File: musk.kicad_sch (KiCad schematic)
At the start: 56 parts, among them J1 debug-port, J10 Conn_01x06_Male, J3 Conn_01x06_Male, J4 Conn_01x06_Male, J5 Conn_01x06_Male, J6 Conn_01x06_Male, J7 Conn_01x06_Male, J8 Conn_01x06_Male, J9 Conn_01x06_Male, K1 diode-choc, K10 diode-choc, K11 diode-choc, K12 diode-choc, K13 diode-choc, K14 diode-choc, K15 diode-choc, K16 diode-choc, K2 diode-choc, K3 diode-choc, K4 diode-choc, K5 diode-choc, K6 diode-choc, K7 diode-choc, K8 diode-choc, K9 diode-choc, SW1 SW_Push, SW2 RotaryEncoder, U1 MT25QL128ABA1ESE, U2 ms88sf3-nrf52840, U3 LSM6DS3, U8 PMW3610, U9 MCP1804x-1802xMB

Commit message: done
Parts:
- removed H1, H2, H3, H4: bumpon, fusion:bumpon-sunk-hole, symbol Mechanical:MountingHole
- removed SC1: solar, misc:KXOB25-05X3F, symbol Device:Solar_Cell
- added JP2: left right or all, Jumper:SolderJumper-3_P1.3mm_Open_RoundedPad1.0x1.5mm, symbol Jumper:SolderJumper_3_Open
- added K17: diode-choc, pg1232:pg1232-DC, symbol switch:diode-choc
- JP1: value All or none -> left right or all
- K13: footprint pg1232:pg1232-DSS -> pg1232:pg1232-DC
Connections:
- net +3V3: now also JP1.2 (C), JP2.3 (B); no longer JP1.1 (A)
- net 3V3_nRF: now also JP1.1 (A)
- net C0: now also K13.2; no longer J5.1 (Pin_1)
- net GND: now also J5.2 (Pin_2); no longer J8.6 (Pin_6), SW1.2
- net R3: now also J8.4 (Pin_4), K13.1, U2.40 (P0.15); no longer J5.2 (Pin_2), J8.3 (Pin_3), U2.41 (P0.17)
- net SOLAR: no longer J8.5 (Pin_5)
- net SOLAR_OUT: now also U9.3 (IN), JP2.1 (A)
- net VDDH: now also JP2.2 (C); no longer JP1.2 (C), U9.3 (IN)
- net ~{BLUE}: now also U2.17 (P0.26); no longer U2.15 (A3_P0.05)
- net ~{RED}: now also U2.15 (A3_P0.05); no longer U2.17 (P0.26)
- net at J9.3 (Pin_3), K16.1: now also K17.1
- net at K16.2: now also J9.5 (Pin_5); no longer J9.2 (Pin_2)
- net at J3.3 (Pin_3): now also J6.4 (Pin_4); no longer J6.3 (Pin_3)
- net at J3.4 (Pin_4): now also J6.3 (Pin_3); no longer J6.4 (Pin_4)
- net at J6.5 (Pin_5): now also J3.2 (Pin_2); no longer J3.5 (Pin_5)
- net at J6.6 (Pin_6): now also J3.1 (Pin_1); no longer J3.6 (Pin_6)
- net at SW1.1: now also J3.6 (Pin_6), J6.1 (Pin_1); no longer U2.28 (P0.18/RST)
- net at J10.3 (Pin_3), K15.1: now also J7.4 (Pin_4); no longer J7.3 (Pin_3)
- net at J7.1 (Pin_1), K15.2: now also J10.6 (Pin_6); no longer J10.1 (Pin_1)
- net at J9.4 (Pin_4): now also K17.2
- net at J10.2 (Pin_2): now also J7.5 (Pin_5); no longer J7.2 (Pin_2)
- net at J10.4 (Pin_4): now also J7.3 (Pin_3)
- net at J10.5 (Pin_5): now also J7.2 (Pin_2); no longer J7.5 (Pin_5)
- net at J7.6 (Pin_6): now also J10.1 (Pin_1); no longer J10.6 (Pin_6)
- new net: J3.5 (Pin_5), J6.2 (Pin_2), SW1.2
- new net C4: J8.3 (Pin_3), U2.41 (P0.17)
- new net RST: J5.1 (Pin_1), U2.28 (P0.18/RST)
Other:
- sheet power ports: added SOLAR; removed VDDH
- note added: "JP1 JP2 12 12 # some DC/DC, some LDO 23 12 # all use builtin DC/DC 123 23 # all using LDO"
- note removed: "- capacitive for hand detection"
- moved on the sheet: C10, C11, C12, C13, C14, C15, J10, JP1, K13, SW1, U8, U9

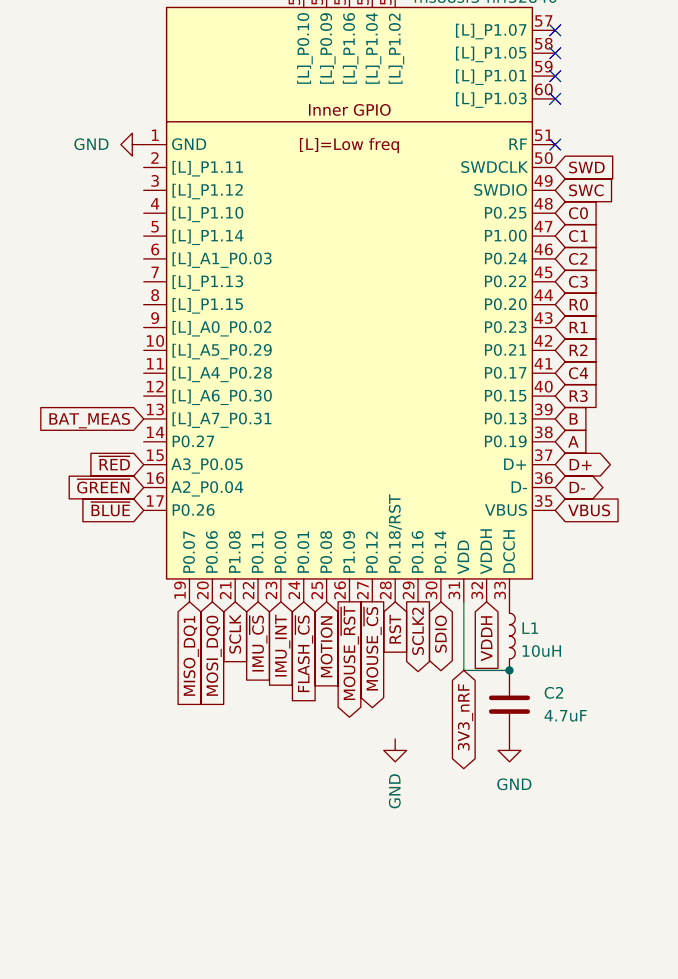
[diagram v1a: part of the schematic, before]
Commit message: 5 thumb cluster
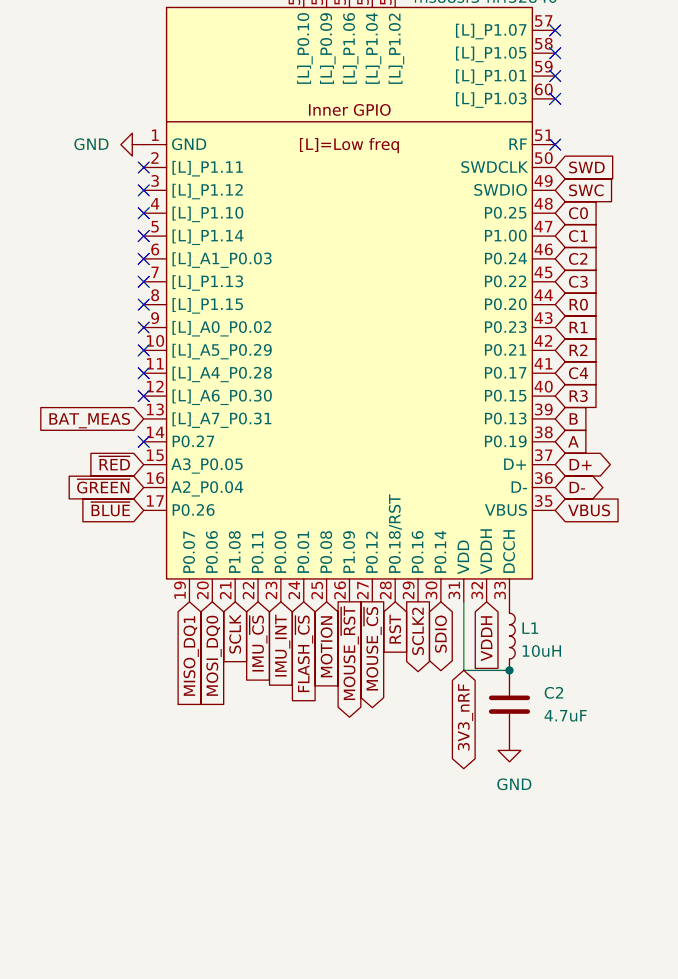
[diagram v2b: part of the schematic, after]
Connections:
- no-connect marks 18 -> 30
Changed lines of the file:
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@@
   (no_connect (at 74.93 29.21))
   (no_connect (at 209.55 110.49))
+  (no_connect (at 29.21 67.31))
+  (no_connect (at 29.21 69.85))
   (no_connect (at 57.15 24.13))
+  (no_connect (at 29.21 52.07))
+  (no_connect (at 29.21 74.93))
+  (no_connect (at 29.21 59.69))
+  (no_connect (at 29.21 44.45))
   (no_connect (at 54.61 24.13))
   (no_connect (at 130.81 124.46))
   (no_connect (at 246.38 120.65))
+  (no_connect (at 29.21 57.15))
   (no_connect (at 269.24 120.65))
   (no_connect (at 52.07 24.13))
+  (no_connect (at 29.21 54.61))
   (no_connect (at 74.93 31.75))
+  (no_connect (at 29.21 62.23))
   (no_connect (at 46.99 24.13))
+  (no_connect (at 29.21 64.77))
   (no_connect (at 74.93 41.91))
   (no_connect (at 74.93 36.83))
@@
   (no_connect (at 269.24 110.49))
   (no_connect (at 209.55 113.03))
+  (no_connect (at 29.21 46.99))
   (no_connect (at 269.24 123.19))
   (no_connect (at 246.38 123.19))
   (no_connect (at 49.53 24.13))
+  (no_connect (at 29.21 49.53))
   (wire (pts (xy 269.24 115.57) (xy 280.67 115.57))
     (stroke (width 0) (type default) (color 0 0 0 0))
@@
     (pin "2")
   )
-  (symbol (lib_id "power:GND") (at 57.15 107.95 0) (unit 1)
-    (in_bom yes) (on_board yes)
-    (property "Reference" "#PWR05" (id 0) (at 57.15 114.3 0)
-      (effects (font (size 1.27 1.27)) hide)
-    )
-    (property "Value" "GND" (id 1) (at 57.15 111.76 90)
-      (effects (font (size 1.27 1.27)) (justify right))
-    )
-    (property "Footprint" "" (id 2) (at 57.15 107.95 0)
-      (effects (font (size 1.27 1.27)) hide)
-    )
-    (property "Datasheet" "" (id 3) (at 57.15 107.95 0)
-      (effects (font (size 1.27 1.27)) hide)
-    )
-    (pin "1")
-  )
   (symbol (lib_id "switch:diode-choc") (at 180.34 132.08 0) (unit 1)
     (in_bom yes) (on_board yes)
@@
       (reference "#PWR04") (unit 1) (value "GND") (footprint "")
     )
-    (path "/9c3a6b82-7222-44b1-a8fb-55963f13e302"
-      (reference "#PWR05") (unit 1) (value "GND") (footprint "")
-    )
     (path "/ee3392d2-a129-45fe-8b02-43c63760b23d"

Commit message: hotswap choc mini
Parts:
- K1, K5, K9: footprint pg1232:pg1232-DCR -> pg1232:pg1232-DHCR
- K10, K13, K14, K15, K16, K17, K2, K6: footprint pg1232:pg1232-DC -> pg1232:pg1232-DHC
- K11, K3, K7: footprint pg1232:pg1232-DCL -> pg1232:pg1232-DHCL
- K12, K4, K8: footprint pg1232:pg1232-DCN -> pg1232:pg1232-DHCN
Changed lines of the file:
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@@
       (effects (font (size 1.27 1.27)) (justify left) hide)
     )
-    (property "Footprint" "pg1232:pg1232-DC" (id 2) (at 278.13 105.41 0)
+    (property "Footprint" "pg1232:pg1232-DHC" (id 2) (at 278.13 105.41 0)
       (effects (font (size 1.27 1.27)) hide)
     )
@@
       (effects (font (size 1.27 1.27)) (justify left) hide)
     )
-    (property "Footprint" "pg1232:pg1232-DC" (id 2) (at 284.48 114.3 0)
+    (property "Footprint" "pg1232:pg1232-DHC" (id 2) (at 284.48 114.3 0)
       (effects (font (size 1.27 1.27)) hide)
     )
@@
       (effects (font (size 1.27 1.27)) (justify left) hide)
     )
-    (property "Footprint" "pg1232:pg1232-DC" (id 2) (at 153.67 137.16 0)
+    (property "Footprint" "pg1232:pg1232-DHC" (id 2) (at 153.67 137.16 0)
       (effects (font (size 1.27 1.27)) hide)
     )
@@
       (effects (font (size 1.27 1.27)) (justify left) hide)
     )
-    (property "Footprint" "pg1232:pg1232-DCR" (id 2) (at 153.67 128.27 0)
+    (property "Footprint" "pg1232:pg1232-DHCR" (id 2) (at 153.67 128.27 0)
       (effects (font (size 1.27 1.27)) hide)
     )
@@
       (effects (font (size 1.27 1.27)) (justify left) hide)
     )
-    (property "Footprint" "pg1232:pg1232-DC" (id 2) (at 261.62 100.33 0)
+    (property "Footprint" "pg1232:pg1232-DHC" (id 2) (at 261.62 100.33 0)
       (effects (font (size 1.27 1.27)) hide)
     )
@@
       (effects (font (size 1.27 1.27)) (justify left) hide)
     )
-    (property "Footprint" "pg1232:pg1232-DCN" (id 2) (at 180.34 119.38 0)
+    (property "Footprint" "pg1232:pg1232-DHCN" (id 2) (at 180.34 119.38 0)
       (effects (font (size 1.27 1.27)) hide)
     )
@@
       (effects (font (size 1.27 1.27)) (justify left) hide)
     )
-    (property "Footprint" "pg1232:pg1232-DCR" (id 2) (at 153.67 110.49 0)
+    (property "Footprint" "pg1232:pg1232-DHCR" (id 2) (at 153.67 110.49 0)
       (effects (font (size 1.27 1.27)) hide)
     )
@@
       (effects (font (size 1.27 1.27)) (justify left) hide)
     )
-    (property "Footprint" "pg1232:pg1232-DCN" (id 2) (at 180.34 128.27 0)
+    (property "Footprint" "pg1232:pg1232-DHCN" (id 2) (at 180.34 128.27 0)
       (effects (font (size 1.27 1.27)) hide)
     )
@@
       (effects (font (size 1.27 1.27)) (justify left) hide)
     )
-    (property "Footprint" "pg1232:pg1232-DCR" (id 2) (at 153.67 119.38 0)
+    (property "Footprint" "pg1232:pg1232-DHCR" (id 2) (at 153.67 119.38 0)
       (effects (font (size 1.27 1.27)) hide)
     )
@@
       (effects (font (size 1.27 1.27)) (justify left) hide)
     )
-    (property "Footprint" "pg1232:pg1232-DC" (id 2) (at 162.56 137.16 0)
+    (property "Footprint" "pg1232:pg1232-DHC" (id 2) (at 162.56 137.16 0)
       (effects (font (size 1.27 1.27)) hide)
     )
@@
       (effects (font (size 1.27 1.27)) (justify left) hide)
     )
-    (property "Footprint" "pg1232:pg1232-DCL" (id 2) (at 171.45 119.38 0)
+    (property "Footprint" "pg1232:pg1232-DHCL" (id 2) (at 171.45 119.38 0)
       (effects (font (size 1.27 1.27)) hide)
     )
@@
       (effects (font (size 1.27 1.27)) (justify left) hide)
     )
-    (property "Footprint" "pg1232:pg1232-DCL" (id 2) (at 171.45 128.27 0)
+    (property "Footprint" "pg1232:pg1232-DHCL" (id 2) (at 171.45 128.27 0)
       (effects (font (size 1.27 1.27)) hide)
     )
@@
       (effects (font (size 1.27 1.27)) (justify left) hide)
     )
-    (property "Footprint" "pg1232:pg1232-DCL" (id 2) (at 171.45 110.49 0)
+    (property "Footprint" "pg1232:pg1232-DHCL" (id 2) (at 171.45 110.49 0)
       (effects (font (size 1.27 1.27)) hide)
     )
@@
       (effects (font (size 1.27 1.27)) (justify left) hide)
     )
-    (property "Footprint" "pg1232:pg1232-DC" (id 2) (at 162.56 110.49 0)
+    (property "Footprint" "pg1232:pg1232-DHC" (id 2) (at 162.56 110.49 0)
       (effects (font (size 1.27 1.27)) hide)
     )
@@
       (effects (font (size 1.27 1.27)) (justify left) hide)
     )
-    (property "Footprint" "pg1232:pg1232-DCN" (id 2) (at 180.34 110.49 0)
+    (property "Footprint" "pg1232:pg1232-DHCN" (id 2) (at 180.34 110.49 0)
       (effects (font (size 1.27 1.27)) hide)
     )
@@
       (effects (font (size 1.27 1.27)) (justify left) hide)
     )
-    (property "Footprint" "pg1232:pg1232-DC" (id 2) (at 162.56 128.27 0)
+    (property "Footprint" "pg1232:pg1232-DHC" (id 2) (at 162.56 128.27 0)
       (effects (font (size 1.27 1.27)) hide)
     )
@@
       (effects (font (size 1.27 1.27)) (justify left) hide)
     )
-    (property "Footprint" "pg1232:pg1232-DC" (id 2) (at 162.56 119.38 0)
+    (property "Footprint" "pg1232:pg1232-DHC" (id 2) (at 162.56 119.38 0)
       (effects (font (size 1.27 1.27)) hide)
     )
@@
     )
     (path "/87bdc01e-a055-4d4c-8488-cd7ca475e086"
-      (reference "K1") (unit 1) (value "diode-choc") (footprint "pg1232:pg1232-DCR")
+      (reference "K1") (unit 1) (value "diode-choc") (footprint "pg1232:pg1232-DHCR")
     )
     (path "/da248da7-bb82-42ca-90ae-06208c9de7f0"
-      (reference "K2") (unit 1) (value "diode-choc") (footprint "pg1232:pg1232-DC")
+      (reference "K2") (unit 1) (value "diode-choc") (footprint "pg1232:pg1232-DHC")
     )
     (path "/d9459f95-47ce-4f40-805c-323d6f49037e"
-      (reference "K3") (unit 1) (value "diode-choc") (footprint "pg1232:pg1232-DCL")
+      (reference "K3") (unit 1) (value "diode-choc") (footprint "pg1232:pg1232-DHCL")
     )
     (path "/ec136a70-3607-4003-a7a6-cdc612bb426c"
-      (reference "K4") (unit 1) (value "diode-choc") (footprint "pg1232:pg1232-DCN")
+      (reference "K4") (unit 1) (value "diode-choc") (footprint "pg1232:pg1232-DHCN")
     )
     (path "/a188b754-8ecd-4d74-8170-d4a8926c87ae"
-      (reference "K5") (unit 1) (value "diode-choc") (footprint "pg1232:pg1232-DCR")
+      (reference "K5") (unit 1) (value "diode-choc") (footprint "pg1232:pg1232-DHCR")
     )
     (path "/f92feeaa-c2da-458b-82e9-a07def69cb43"
-      (reference "K6") (unit 1) (value "diode-choc") (footprint "pg1232:pg1232-DC")
+      (reference "K6") (unit 1) (value "diode-choc") (footprint "pg1232:pg1232-DHC")
     )
     (path "/ae452cd4-a096-4b05-9662-460b8817444e"
-      (reference "K7") (unit 1) (value "diode-choc") (footprint "pg1232:pg1232-DCL")
+      (reference "K7") (unit 1) (value "diode-choc") (footprint "pg1232:pg1232-DHCL")
     )
     (path "/7963e912-fe67-47e1-8f51-4cb8ba56eb8c"
-      (reference "K8") (unit 1) (value "diode-choc") (footprint "pg1232:pg1232-DCN")
+      (reference "K8") (unit 1) (value "diode-choc") (footprint "pg1232:pg1232-DHCN")
     )
     (path "/45b4d680-79c6-462d-8620-4846ae703fd9"
-      (reference "K9") (unit 1) (value "diode-choc") (footprint "pg1232:pg1232-DCR")
+      (reference "K9") (unit 1) (value "diode-choc") (footprint "pg1232:pg1232-DHCR")
     )
     (path "/f3d11e68-ea73-47b6-a5c5-7f172924a5ac"
-      (reference "K10") (unit 1) (value "diode-choc") (footprint "pg1232:pg1232-DC")
+      (reference "K10") (unit 1) (value "diode-choc") (footprint "pg1232:pg1232-DHC")
     )
     (path "/cb60c373-da5a-49e5-a01f-0bb47bd19c8a"
-      (reference "K11") (unit 1) (value "diode-choc") (footprint "pg1232:pg1232-DCL")
+      (reference "K11") (unit 1) (value "diode-choc") (footprint "pg1232:pg1232-DHCL")
     )
     (path "/9c60c31c-8d19-4129-96ae-58b8c24f361a"
-      (reference "K12") (unit 1) (value "diode-choc") (footprint "pg1232:pg1232-DCN")
+      (reference "K12") (unit 1) (value "diode-choc") (footprint "pg1232:pg1232-DHCN")
     )
     (path "/360112f0-6f4f-4683-9f67-c30cff64c0d6"
-      (reference "K13") (unit 1) (value "diode-choc") (footprint "pg1232:pg1232-DC")
+      (reference "K13") (unit 1) (value "diode-choc") (footprint "pg1232:pg1232-DHC")
     )
     (path "/abfa173d-9db1-45b6-ad22-b6c38a35afa9"
-      (reference "K14") (unit 1) (value "diode-choc") (footprint "pg1232:pg1232-DC")
+      (reference "K14") (unit 1) (value "diode-choc") (footprint "pg1232:pg1232-DHC")
     )
     (path "/700f52c5-679c-497f-8976-e17d015dbeaa"
-      (reference "K15") (unit 1) (value "diode-choc") (footprint "pg1232:pg1232-DC")
+      (reference "K15") (unit 1) (value "diode-choc") (footprint "pg1232:pg1232-DHC")
     )
     (path "/01126c3f-c4a5-40d4-b9ca-b1499249e4e6"
-      (reference "K16") (unit 1) (value "diode-choc") (footprint "pg1232:pg1232-DC")
+      (reference "K16") (unit 1) (value "diode-choc") (footprint "pg1232:pg1232-DHC")
     )
     (path "/19823ff2-d2db-4ee5-aacd-d1824e0bc3d9"
-      (reference "K17") (unit 1) (value "diode-choc") (footprint "pg1232:pg1232-DC")
+      (reference "K17") (unit 1) (value "diode-choc") (footprint "pg1232:pg1232-DHC")
     )
     (path "/df110090-d77e-4643-a152-1c756b2f3a70"

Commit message: swap bms and reg
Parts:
- removed C1: 10nF, Capacitor_SMD:C_0603_1608Metric, symbol Device:C
- removed U9: MCP1804x-1802xMB, Package_TO_SOT_SMD:SOT-89-3, symbol Regulator_Linear:MCP1804x-1802xMB
- added D1: RED, LED_SMD:LED_0805_2012Metric, symbol Device:LED
- added R11: 1k, Resistor_SMD:R_0603_1608Metric, symbol Device:R
- C12: value 100uF -> 100nF
- K1, K10, K11, K12, K14, K15, K16, K17, K2, K3, K4, K5, K6, K7, K8, K9: lcsc-part (none) -> C64898
- R2, R3: value 5.1M -> 100k
- U1: value MT25QL128ABA1ESE -> W25Q128
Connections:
- net SOLAR_OUT is gone; now on net VDDH_OUT: JP2.1 (A)
- net GND: no longer R3.2
- net BAT_MEAS_EN: now reaches U2.14 (P0.27)
- net BAT_MEAS_EN: now also R3.2
- net at J9.1 (Pin_1): now also D1.1 (K)
- net at J9.2 (Pin_2): now also D1.2 (A)
- net VDDH_OUT: now reaches J8.5 (Pin_5)
- net at J8.6 (Pin_6): now also R11.2
- new net ~{CHG}: R11.1
- no-connect marks 30 -> 25
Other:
- sheet power ports: added 1V8, BAT, VDDH, ~{CHG}; removed CAP, SOLAR, SOLAR_OUT
- moved on the sheet: K17

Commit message: top
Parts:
- J10, J3, J4, J5, J6, J7, J8, J9: value Conn_01x06_Male -> bridge
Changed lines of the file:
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@@
       (effects (font (size 1.27 1.27)) (justify right))
     )
-    (property "Value" "Conn_01x06_Male" (id 1) (at 238.76 125.73 0)
+    (property "Value" "bridge" (id 1) (at 238.76 125.73 0)
       (effects (font (size 1.27 1.27)) (justify right))
     )
@@
       (effects (font (size 1.27 1.27)) (justify right))
     )
-    (property "Value" "Conn_01x06_Male" (id 1) (at 226.06 107.95 0)
+    (property "Value" "bridge" (id 1) (at 226.06 107.95 0)
       (effects (font (size 1.27 1.27)) (justify right))
     )
@@
       (effects (font (size 1.27 1.27)) (justify right))
     )
-    (property "Value" "Conn_01x06_Male" (id 1) (at 203.2 125.73 0)
+    (property "Value" "bridge" (id 1) (at 203.2 125.73 0)
       (effects (font (size 1.27 1.27)) (justify right))
     )
@@
       (effects (font (size 1.27 1.27)) (justify right))
     )
-    (property "Value" "Conn_01x06_Male" (id 1) (at 275.59 107.95 0)
+    (property "Value" "bridge" (id 1) (at 275.59 107.95 0)
       (effects (font (size 1.27 1.27)) (justify right))
     )
@@
       (effects (font (size 1.27 1.27)) (justify right))
     )
-    (property "Value" "Conn_01x06_Male" (id 1) (at 215.9 125.73 0)
+    (property "Value" "bridge" (id 1) (at 215.9 125.73 0)
       (effects (font (size 1.27 1.27)) (justify right))
     )
@@
       (effects (font (size 1.27 1.27)) (justify right))
     )
-    (property "Value" "Conn_01x06_Male" (id 1) (at 252.73 107.95 0)
+    (property "Value" "bridge" (id 1) (at 252.73 107.95 0)
       (effects (font (size 1.27 1.27)) (justify right))
     )
@@
       (effects (font (size 1.27 1.27)) (justify right))
     )
-    (property "Value" "Conn_01x06_Male" (id 1) (at 262.89 125.73 0)
+    (property "Value" "bridge" (id 1) (at 262.89 125.73 0)
       (effects (font (size 1.27 1.27)) (justify right))
     )
@@
       (effects (font (size 1.27 1.27)) (justify right))
     )
-    (property "Value" "Conn_01x06_Male" (id 1) (at 240.03 125.73 0)
+    (property "Value" "bridge" (id 1) (at 240.03 125.73 0)
       (effects (font (size 1.27 1.27)) (justify right))
     )
@@
     )
     (path "/13ba9cc6-feab-41e2-9f0a-09c409038987"
-      (reference "J3") (unit 1) (value "Conn_01x06_Male") (footprint "musk:bridge")
+      (reference "J3") (unit 1) (value "bridge") (footprint "musk:bridge")
     )
     (path "/25c29169-6ec4-4a25-979d-f596fdc044b9"
-      (reference "J4") (unit 1) (value "Conn_01x06_Male") (footprint "musk:bridge")
+      (reference "J4") (unit 1) (value "bridge") (footprint "musk:bridge")
     )
     (path "/12471d44-d3bf-4128-b847-f56e537242a3"
-      (reference "J5") (unit 1) (value "Conn_01x06_Male") (footprint "musk:bridge")
+      (reference "J5") (unit 1) (value "bridge") (footprint "musk:bridge")
     )
     (path "/b2e6f337-4797-4755-922d-10208728ffa5"
-      (reference "J6") (unit 1) (value "Conn_01x06_Male") (footprint "musk:bridge")
+      (reference "J6") (unit 1) (value "bridge") (footprint "musk:bridge")
     )
     (path "/cf5489a3-2bc4-4cd6-82dd-5ed37be5af94"
-      (reference "J7") (unit 1) (value "Conn_01x06_Male") (footprint "musk:bridge")
+      (reference "J7") (unit 1) (value "bridge") (footprint "musk:bridge")
     )
     (path "/fb87447a-5a57-41b1-b7c4-4666568e2348"
-      (reference "J8") (unit 1) (value "Conn_01x06_Male") (footprint "musk:bridge")
+      (reference "J8") (unit 1) (value "bridge") (footprint "musk:bridge")
     )
     (path "/84f91bd3-e4aa-4fcd-b902-b31e694e11f1"
-      (reference "J9") (unit 1) (value "Conn_01x06_Male") (footprint "musk:bridge")
+      (reference "J9") (unit 1) (value "bridge") (footprint "musk:bridge")
     )
     (path "/bde858d9-fa44-47e3-aa4a-29083efd5e88"
-      (reference "J10") (unit 1) (value "Conn_01x06_Male") (footprint "musk:bridge")
+      (reference "J10") (unit 1) (value "bridge") (footprint "musk:bridge")
     )
     (path "/06e79cfb-e062-456a-915a-aac3339d9f3e"
